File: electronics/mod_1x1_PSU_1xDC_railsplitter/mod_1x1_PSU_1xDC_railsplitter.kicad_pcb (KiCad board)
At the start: 2 copper layers, 42.5 x 46.2 mm, 53 parts, among them J1 module_2x15_left_input, J2 module_2x15_right_input, J3 Jack-DC, J5 Conn_01x02, U1 LD1117, U2 LM317, U3 LM337, U4 LD1117, U5 TLV431

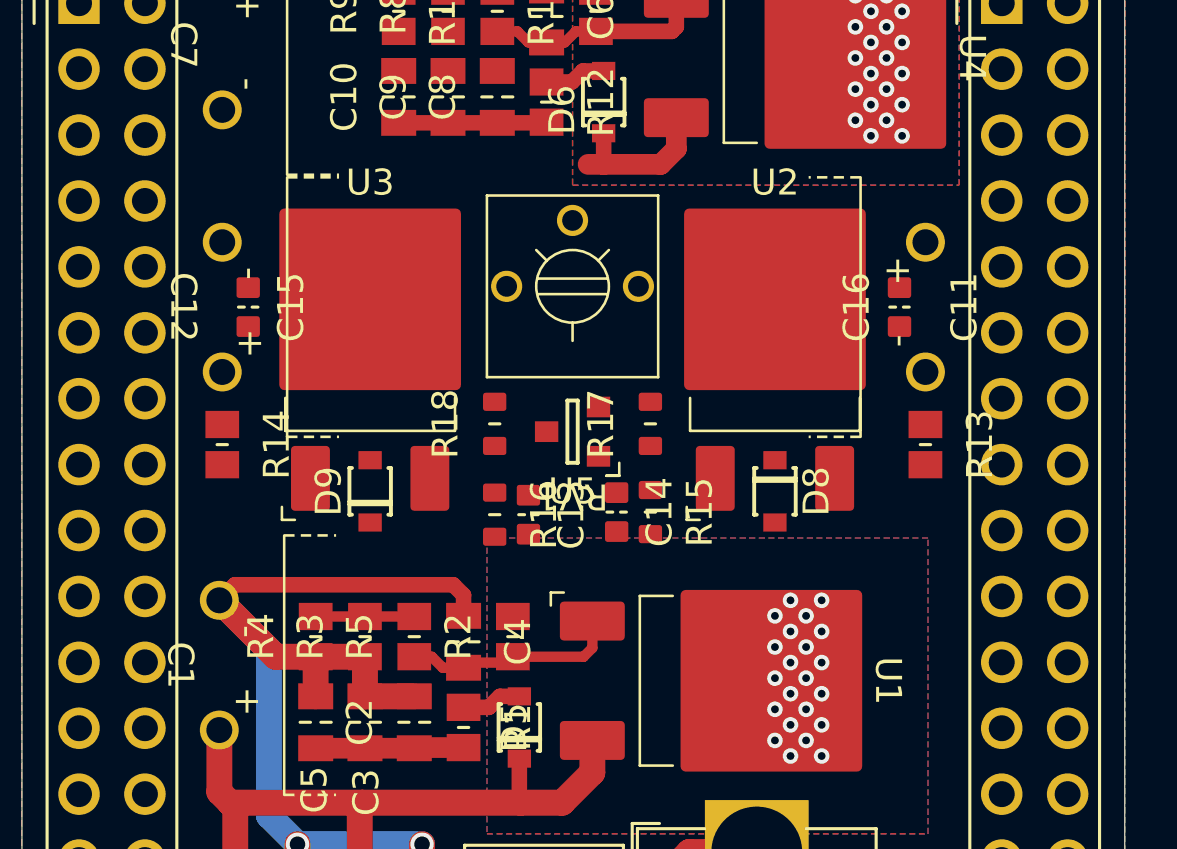
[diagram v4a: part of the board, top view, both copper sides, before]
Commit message: further placing and routing
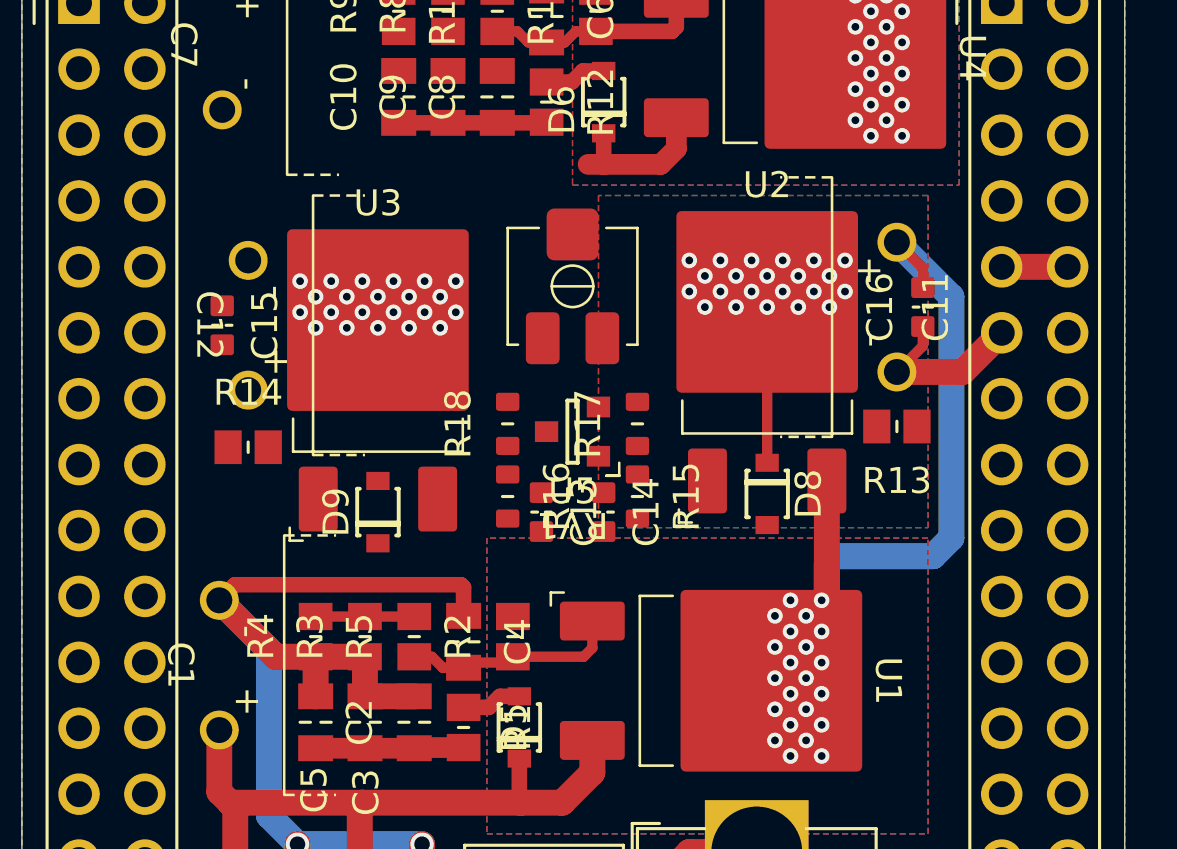
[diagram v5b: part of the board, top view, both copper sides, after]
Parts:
- RV1: footprint SquantorRcl:POT-Bourns-3362P -> SquantorRcl:POT-23A-BI_technologies
- moved R13 1.30 mm to (176.3, 88.7), turned to 180 degrees
- moved C12 1.22 mm to (151.3, 84.8)
- moved C15 1.22 mm to (150.3, 84.8)
- moved C11 1.10 mm to (176.3, 84.1)
- moved R14 1.00 mm to (151.3, 89.5), turned to 0 degrees
- moved C16 0.90 mm to (177.3, 84.1)
- moved R16 0.86 mm to (161.3, 91.4)
- moved D9 0.85 mm to (156.3, 92.0)
- moved U3 0.85 mm to (156.3, 84.6)
- moved R15 0.78 mm to (166.3, 91.4)
- moved C13 0.51 mm to (162.6, 92.0)
- moved C14 0.50 mm to (165.0, 92.0)
- moved R17 0.50 mm to (166.3, 88.6)
- moved R18 0.50 mm to (161.3, 88.6)
- moved U2 0.32 mm to (171.3, 83.9)
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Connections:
- C1 pad 2: /DC1n -> /V-A
- C11 pad 1: VDD -> /V+A
- C12 pad 2: /DC1n -> /V-A
- C13 pad 2: /DC1n -> /V-A
- C14 pad 2: VDD -> /V+A
- C15 pad 1: /DC1n -> /V-A
- C16 pad 2: VDD -> /V+A
- C2 pad 2: /DC1n -> /V-A
- C3 pad 2: /DC1n -> /V-A
- C4 pad 1: /DC1n -> /V-A
- C5 pad 2: /DC1n -> /V-A
- C7 pad 1: VDD -> /V+A
- D2 pad 2: /DC1n -> /V-A
- D4 pad 2: /DC1n -> /V-A
- D5 pad 2: VDD -> /V+A
- D6 pad 1: VDD -> /V+A
- R1 pad 1: VDD -> /V+A
- R15 pad 2: VDD -> /V+A
- R16 pad 2: /DC1n -> /V-A
- R2 pad 2: VDD -> /V+A
- R3 pad 1: /DC1n -> /V-A
- R4 pad 1: /DC1n -> /V-A
- U1 pad 2: VDD -> /V+A
- U3 pad 2: /DC1n -> /V-A
- U4 pad 3: VDD -> /V+A
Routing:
- net /V-A: track 0.00 -> 40.8 mm, vias 0 -> 24
- net /DC1n: track 40.6 -> 0.00 mm, vias 2 -> 0
- net /V+A: track 0.00 -> 37.6 mm, vias 0 -> 22
- net VDD: track 8.37 -> 0.00 mm, vias 22 -> 0
- net GND: track 0.00 -> 6.83 mm
- net Net-(D8-K): track 0.00 -> 6.20 mm, vias 0 -> 22
- net /+5V: track 2.38 -> 4.92 mm
- added copper zone on B.Cu, net /V+A
- added copper zone on F.Cu, net /V+A
- added copper zone on B.Cu, net Net-(D8-K)
- added copper zone on F.Cu, net Net-(D8-K)
- removed copper zone on B.Cu, net VDD
- removed copper zone on F.Cu, net VDD

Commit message: routing completed
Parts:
- moved C6 2.75 mm to (160.2, 72.0)
- moved R12 2.75 mm to (160.2, 75.3)
- moved C10 2.75 mm to (154.5, 75.1)
- moved C8 2.75 mm to (158.3, 75.1)
- moved C9 2.75 mm to (156.4, 75.1)
- moved D6 2.75 mm to (162.4, 75.3)
- moved R10 2.75 mm to (158.3, 71.8)
- moved R11 2.75 mm to (162.1, 71.8)
- moved R8 2.75 mm to (156.4, 71.8)
- moved R9 2.75 mm to (154.5, 71.8)
- moved U4 2.75 mm to (172.1, 73.6)
- moved D9 0.92 mm to (156.9, 91.3)
- moved U3 0.92 mm to (156.9, 83.9)
- moved R14 0.89 mm to (151.9, 88.8)
- moved C12 0.85 mm to (151.9, 84.2)
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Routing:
- net /V-A: track 40.8 -> 104.4 mm
- net /V+A: track 37.6 -> 93.9 mm, vias 22 -> 24
- net /+5V: track 4.92 -> 56.4 mm, vias 22 -> 20
- net Net-(D9-K): track 0.00 -> 15.8 mm
- net Net-(D8-A): track 0.00 -> 14.3 mm
- net GND: track 6.83 -> 17.6 mm
- net Net-(D9-A): track 0.00 -> 10.1 mm
- net Net-(U5-REF): track 0.00 -> 6.87 mm
- net Net-(D8-K): track 6.20 -> 0.00 mm
- net Net-(R18-Pad2): track 0.00 -> 2.92 mm
- net Net-(R17-Pad2): track 0.00 -> 2.92 mm
- added copper zone on B.Cu, net /V-A
- added copper zone on F.Cu, net /V-A

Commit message: completed silk placement, few values adjusted
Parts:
- N1: value 20230924 -> 20231003
- R1, R12: value 1 -> 2.2
- moved N2 31.6 mm to (167.4, 89.0)
- moved C14 0.99 mm to (165.2, 90.9)
- moved R15 0.99 mm to (166.5, 90.9)
- moved R16 0.73 mm to (161.6, 90.9)
- moved C13 0.20 mm to (162.9, 91.6)
- moved C1 0.11 mm to (150.3, 97.9)
- moved C16 0.10 mm to (176.7, 84.2)
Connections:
- U2 pad 3: VDD -> /V+A
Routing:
- net /V+A: track 93.9 -> 99.5 mm
- net Net-(D9-K): track 15.8 -> 17.8 mm
- net Net-(D8-A): track 14.3 -> 13.4 mm

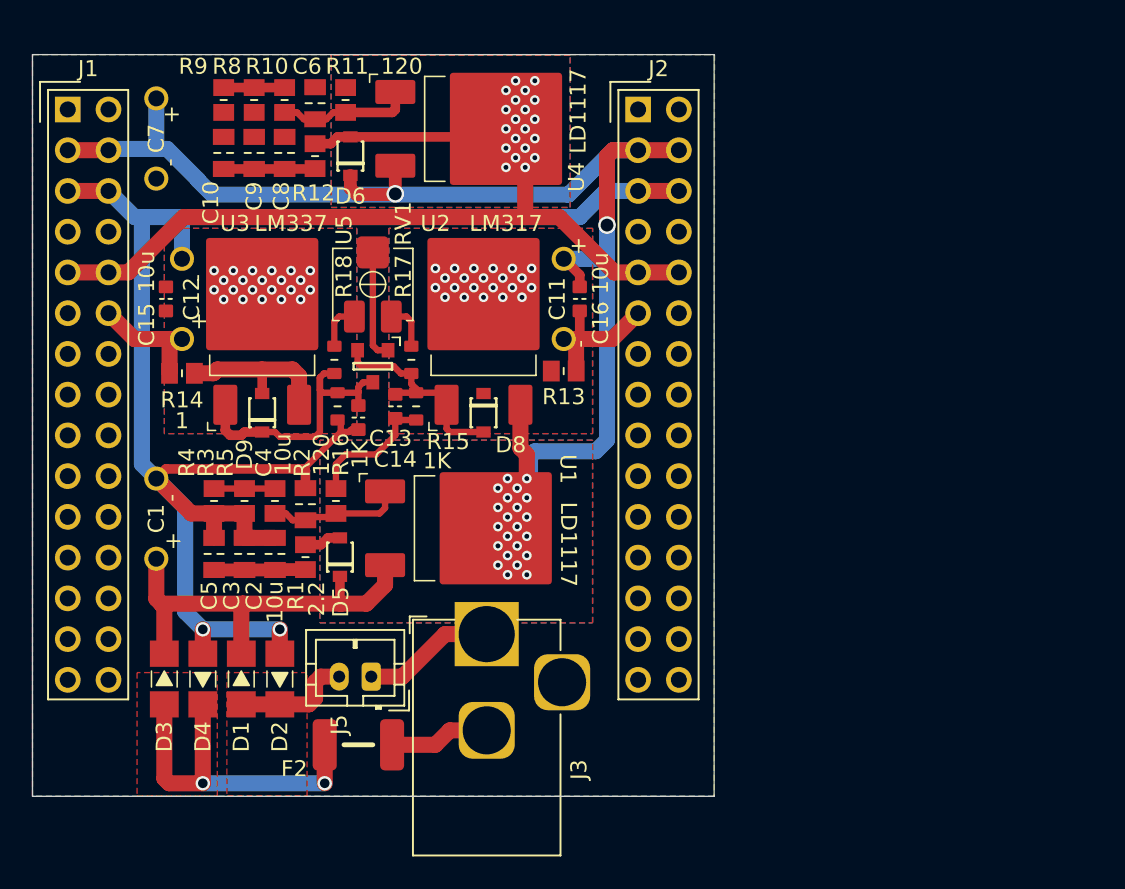
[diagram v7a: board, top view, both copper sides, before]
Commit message: fixing DRC errors
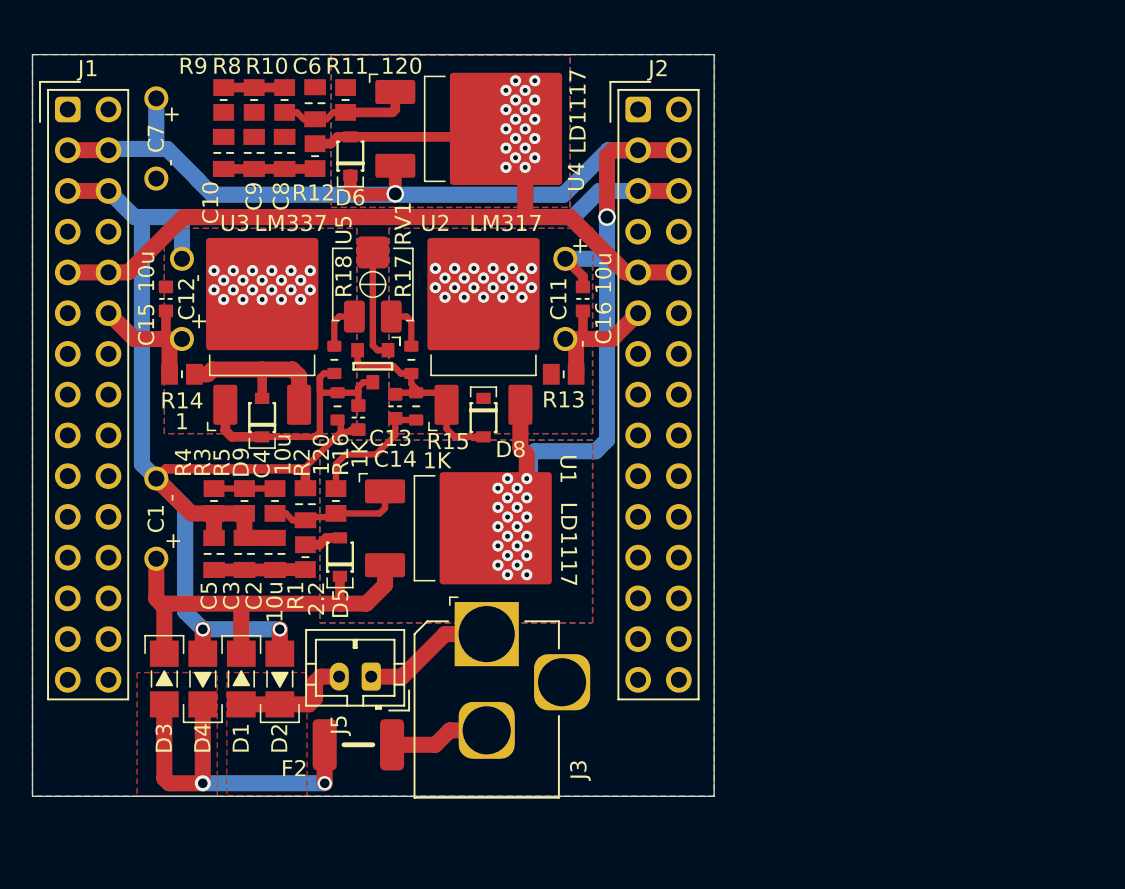
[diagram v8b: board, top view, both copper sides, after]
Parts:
- N1: value 20231003 -> 20231206
- moved D8 0.30 mm to (170.7, 91.6)
- moved D9 0.30 mm to (156.9, 91.6)
- moved C16 0.20 mm to (176.9, 84.2)
- moved R13 0.20 mm to (175.7, 88.9)
- moved C11 0.10 mm to (175.8, 84.2)
- moved R14 0.06 mm to (151.9, 88.9)
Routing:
- net GND: track 17.3 -> 19.3 mm
